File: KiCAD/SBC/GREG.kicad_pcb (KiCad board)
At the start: 2 copper layers, 105 parts, among them J1 Micro_SD_Card_Det1, J10 LIDAR, J11 LCD, J12 ToF1, J13 ToF2, J14 ToF3, J15 ToF4, J16 ToF5, J17 ToF6, J18 Breakouts, J19 Microphone, J2 RJ45_JK0654219, J3 USB_A_Stacked, J4 USB_C_Receptacle_USB2.0_16P, J5 HDMI_A, J6 Camera 1, J7 AudioJack3, J8 DEBUG, J9 Camera 2, SW1 SW_Push, U1 T527M00X0DCH, U2 K4F6E3S4HM-THCL, U3 AXP717B, U4 ICM-45686, U5 RTL8211EG-VB-CG, U6 SN74CBTLV16292GR, U7 TPS61165DBV, U8 TCA9548AMRGER, Y1 25MHz, Y2 24MHz

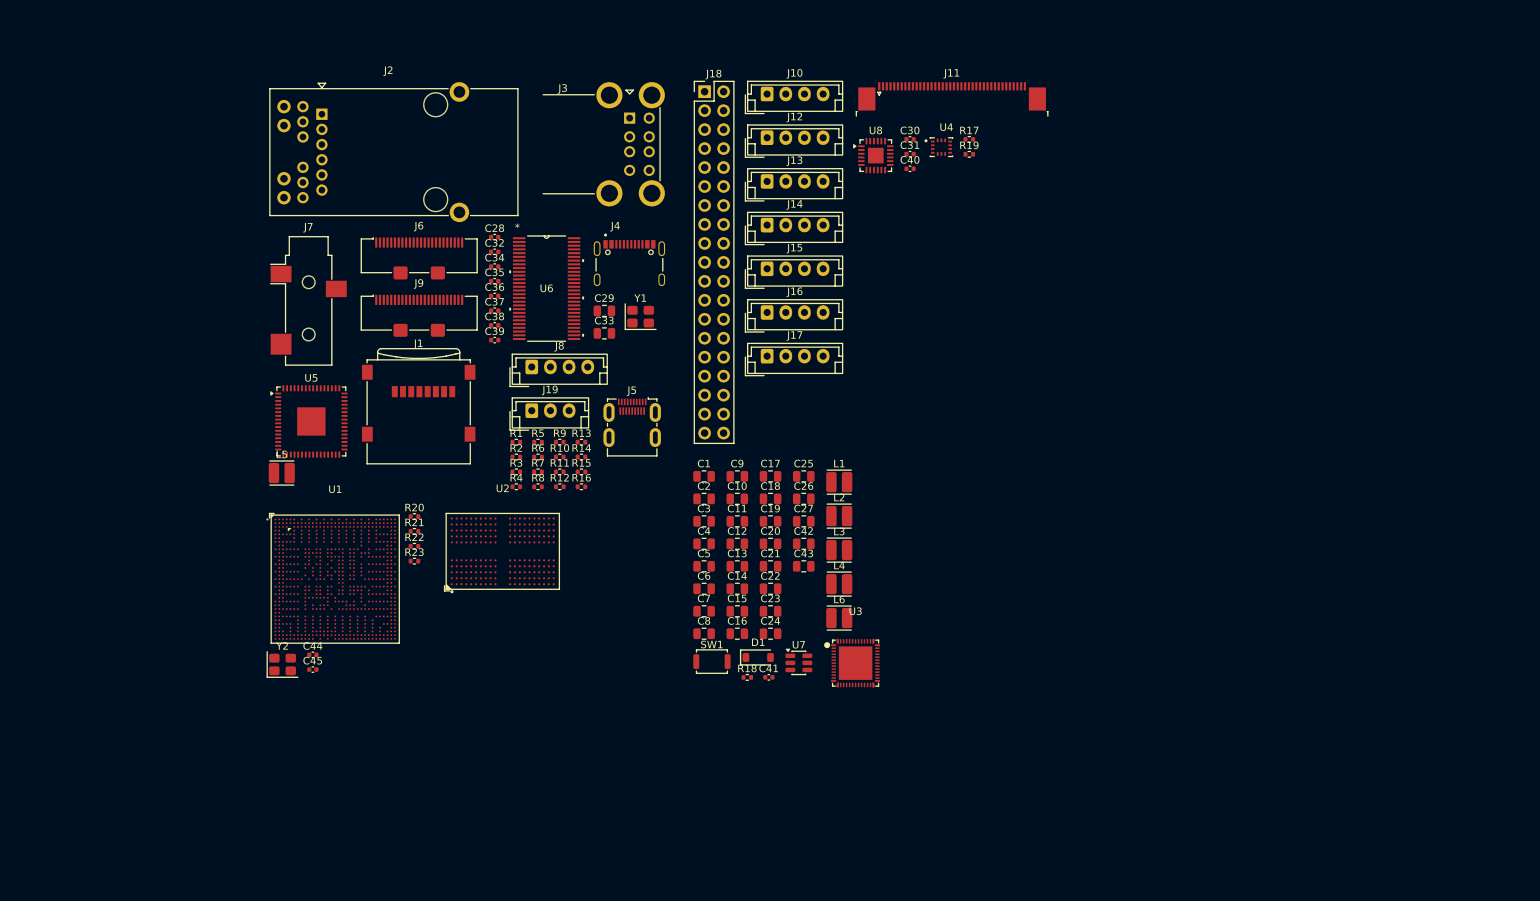
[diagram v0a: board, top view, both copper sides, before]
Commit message: Add journal and update readme
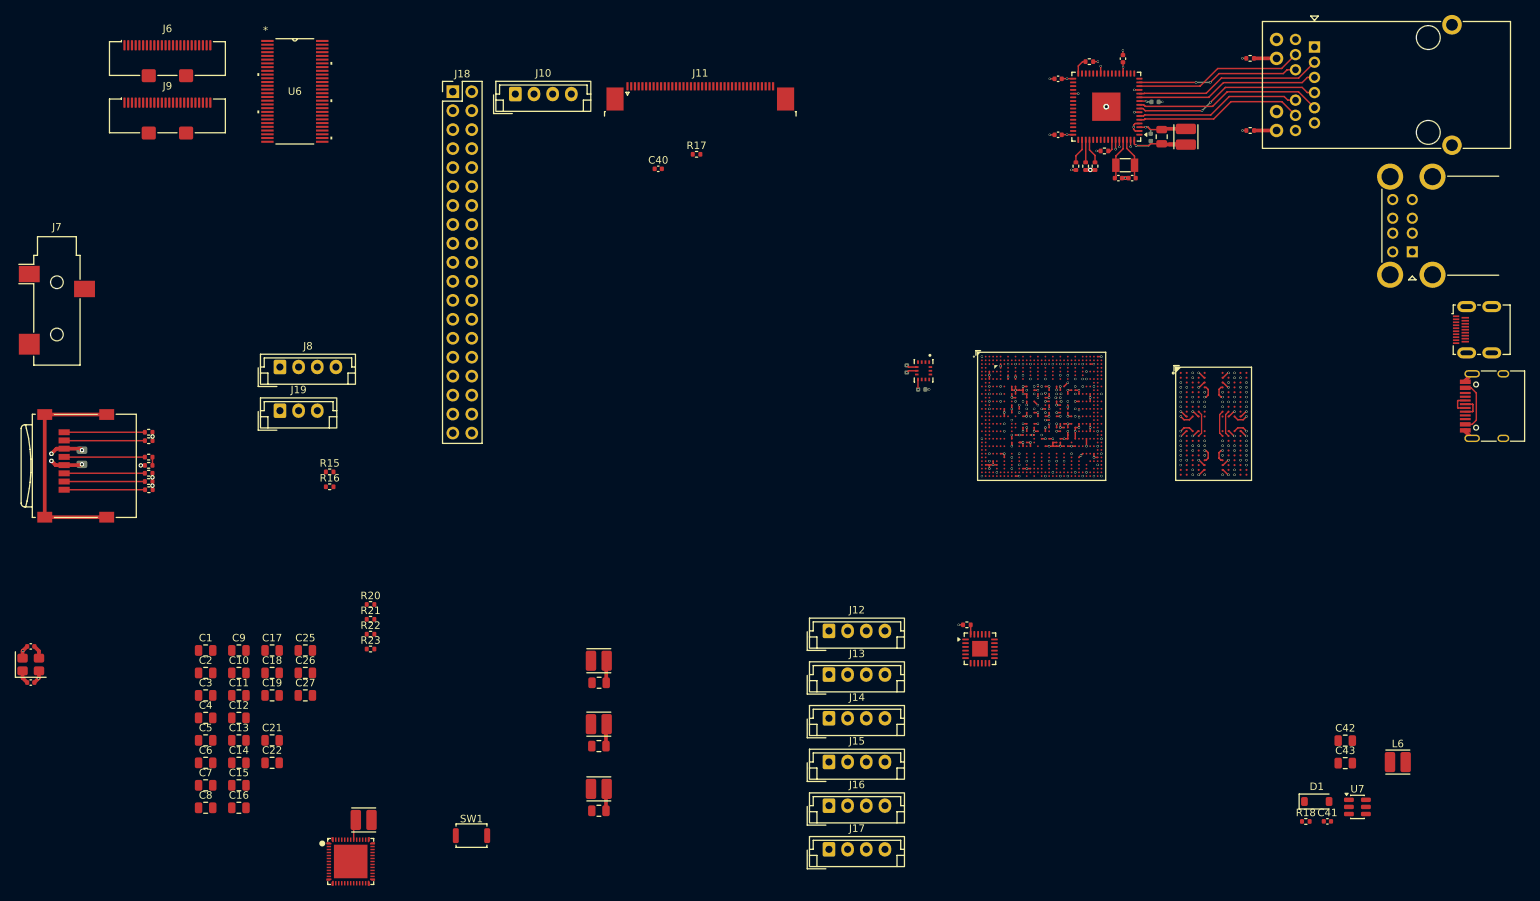
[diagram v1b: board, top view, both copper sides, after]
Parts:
- C28, C29, C30, C31, C32, C34: moved to B.Cu
- J4: footprint USBC:HRO_TYPE-C-31-M-12 -> Connector_USB:USB_C_Receptacle_HRO_TYPE-C-31-M-12
- Y1: footprint Crystal:Crystal_SMD_3225-4Pin_3.2x2.5mm -> Crystal:Crystal_SMD_3215-2Pin_3.2x1.5mm
- moved J2 133.2 mm to (217.8, 42.9)
- moved L5 129.2 mm to (200.5, 54.9), turned to 90 degrees
- moved J4 117.2 mm to (242.0, 91.0), turned to 90 degrees
- moved J5 116.0 mm to (241.5, 80.8), turned to 90 degrees
- moved U5 114.5 mm to (189.9, 50.9), turned to 180 degrees
- moved R8 106.6 mm to (209.2, 54.1)
- moved J3 106.3 mm to (230.9, 70.3), turned to 180 degrees
- moved R9 105.8 mm to (209.1, 44.4)
- moved U1 97.1 mm to (181.2, 92.3)
- moved U2 96.7 mm to (204.2, 93.3), turned to -90 degrees
- moved C34 91.1 mm to (196.4, 50.2)
- moved C35 89.3 mm to (192.1, 44.5), turned to 90 degrees
- moved C32 89.2 mm to (195.8, 55.0), turned to 90 degrees
- moved C38 87.6 mm to (193.3, 60.5), turned to 180 degrees
- moved C39 86.3 mm to (191.5, 60.5)
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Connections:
- J2 pad 1: /Connectivity/CT_COMMON -> unconnected-(J2-MXCT3-Pad1)
- J2 pad 12: /Connectivity/CT_COMMON -> unconnected-(J2-MXCT1-Pad12)
- J2 pad 6: /Connectivity/CT_COMMON -> unconnected-(J2-MXCT2-Pad6)
- J2 pad 7: /Connectivity/CT_COMMON -> unconnected-(J2-MXCT4-Pad7)
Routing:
- net GND: track 0.00 -> 75.8 mm, vias 0 -> 163
- net SD_DET: track 0.00 -> 30.4 mm
- net VDD_DRAM: track 0.00 -> 27.3 mm, vias 0 -> 37
- net /Connectivity/MX2N: track 0.00 -> 25.2 mm
- net /Connectivity/MX3N: track 0.00 -> 25.2 mm
- net /Connectivity/MX2P: track 0.00 -> 25.1 mm, vias 0 -> 2
- net /Connectivity/MX3P: track 0.00 -> 24.5 mm
- net /Connectivity/MX1P: track 0.00 -> 22.7 mm
- net /Connectivity/MX4P: track 0.00 -> 22.7 mm
- net /Connectivity/MX1N: track 0.00 -> 22.2 mm
- net /Connectivity/MX4N: track 0.00 -> 21.6 mm, vias 0 -> 2
- net VCC_3V3: track 0.00 -> 19.8 mm, vias 0 -> 18
- net /Connectivity/VDDREG: track 0.00 -> 12.8 mm, vias 0 -> 1
- net SD_DAT2: track 0.00 -> 10.8 mm
- net SD_DAT0: track 0.00 -> 10.8 mm
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- added copper zone on In1.Cu, net GND
- added copper zone on In7.Cu, net VCC_1V3
- added copper zone on In2.Cu, net VCC_1V8
- added copper zone on In4.Cu, net VCC_3V3
- added copper zone on In8.Cu, net VCC_3V9
- added copper zone on In5.Cu, net VDD_CPU
- added copper zone on In3.Cu, net VDD_DRAM
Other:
- copper layers 2 -> 10
